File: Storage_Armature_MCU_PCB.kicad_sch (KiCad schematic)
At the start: 71 parts, among them Q1 20N06, U14 USBLC6-2P6, U4 ADP3338AKCZ-3.3RL7, U5 ADP3338AKCZ-3.3RL7

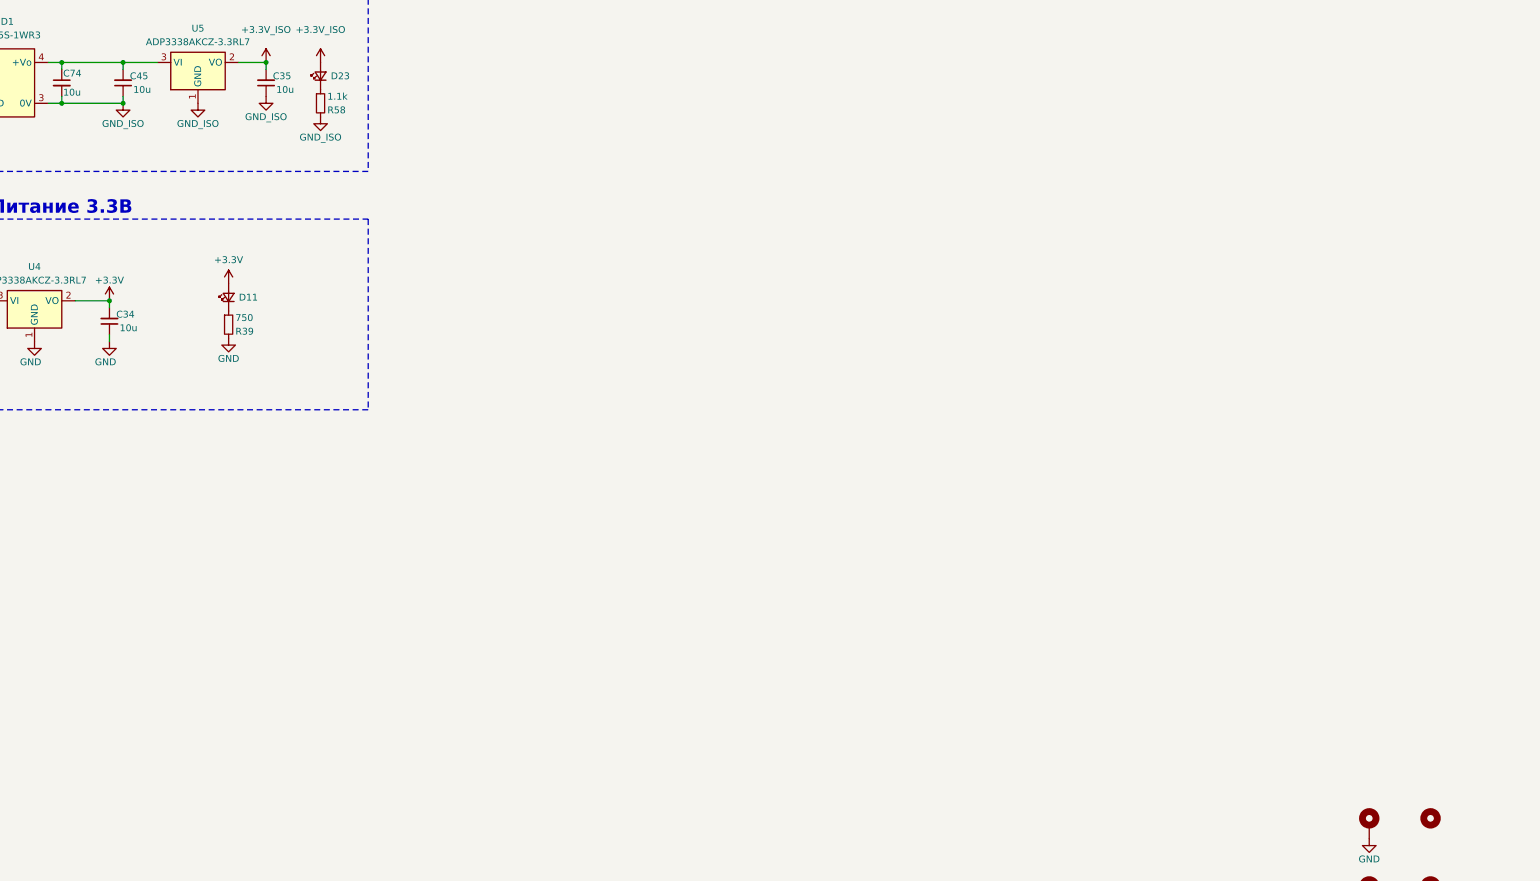
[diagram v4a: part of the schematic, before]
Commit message: VER1.0: объединил земли датчиков и 24В
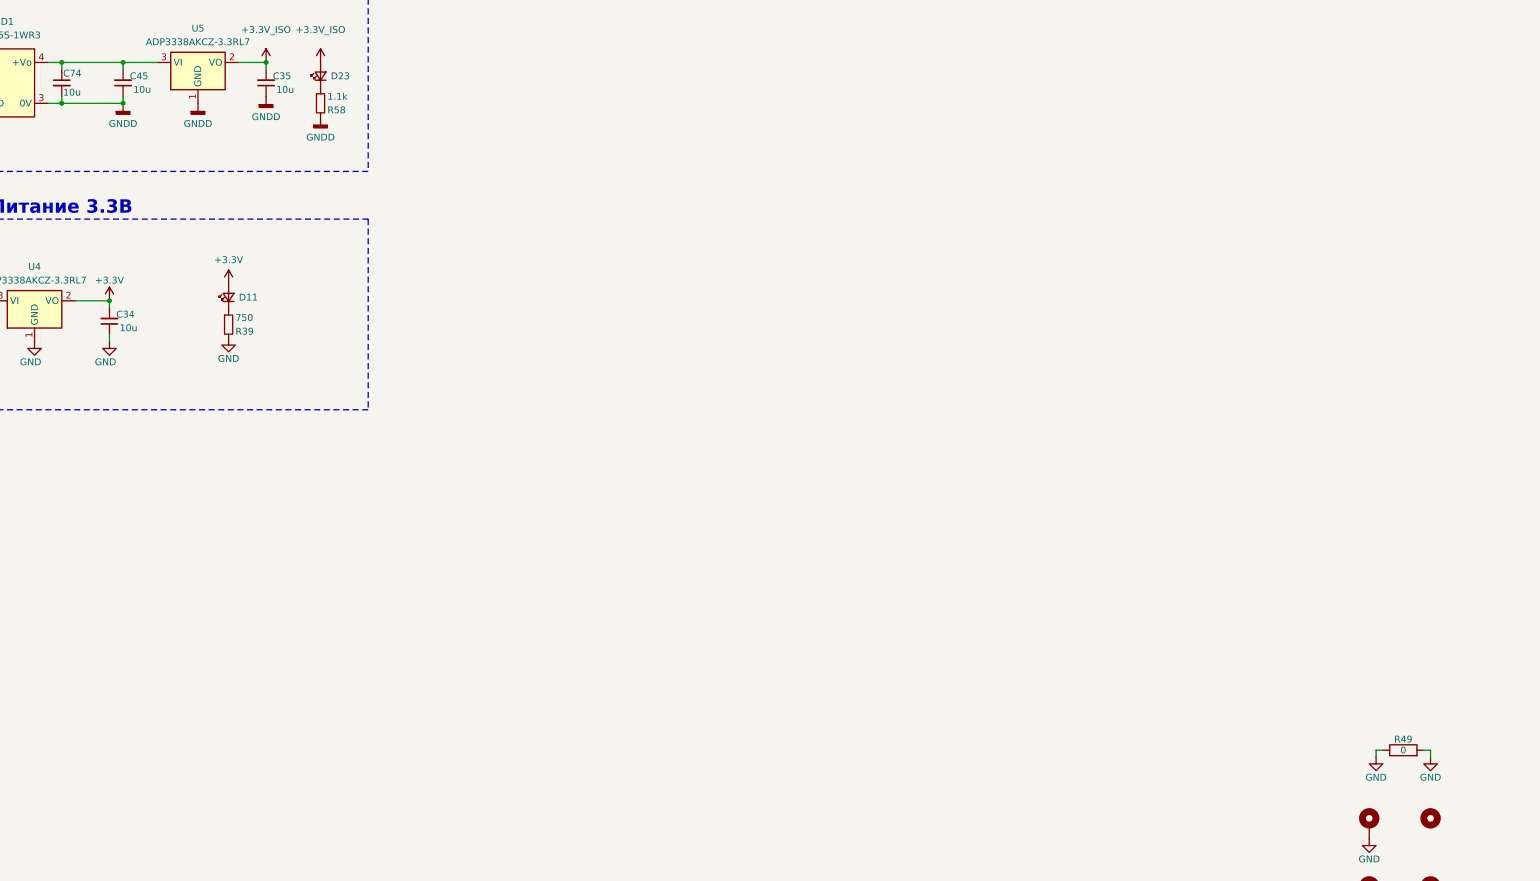
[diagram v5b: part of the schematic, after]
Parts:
- added R49: 0, Resistor_SMD:R_2512_6332Metric_Pad1.40x3.35mm_HandSolder, symbol Device:R
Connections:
- net GND_ISO is gone; now on net GNDD: C35.1, C45.1, C74.2, D1.3 (0V), R58.2, U5.1 (GND)
- net GND: now also R49.1, R49.2

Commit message: VER1.0: добавил светодиоды, тестпоинты и мягкий старт 24В
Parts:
- added Q2: 20N06, Package_TO_SOT_SMD:TO-252-2, symbol Transistor_FET:BSP89
- added R78: 470k, Resistor_SMD:R_0805_2012Metric_Pad1.20x1.40mm_HandSolder, symbol Device:R_Small
- R54: value 8.2k -> 4.7k
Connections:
- net GNDD: now also Q2.2 (D); no longer C70.2, D20.2 (A), Q1.3 (S)
- net Sensor_3/P_measure_MCU: now reaches U1.10 (PC2)
- net Sensor_4/P_measure_MCU: now reaches U1.11 (PC3)
- net Sensor_5/P_measure_MCU: now reaches U1.15 (PA1)
- net Sensor_6/P_measure_MCU: now reaches U1.16 (PA2)
- net Sensor_7/P_measure_MCU: now reaches U1.17 (PA3)
- net Sensor_8/P_measure_MCU: now reaches U1.20 (PA4)
- net Solenoid1_MCU: now reaches U1.50 (PA15)
- net Solenoid2_MCU: now reaches U1.51 (PC10)
- net Solenoid3_MCU: now reaches U1.52 (PC11)
- net Solenoid4_MCU: now reaches U1.53 (PC12)
- net Sensor_1/P_measure_MCU: now reaches U1.8 (PC0)
- net Sensor_2/P_measure_MCU: now reaches U1.9 (PC1)
- net at C70.1, D20.1 (K), Q1.1 (G)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: now also Q2.1 (G), R78.1
- new net: C70.2, D20.2 (A), Q1.3 (S), Q2.3 (S), R78.2
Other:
- added sheet Sensor_6 (Measure.kicad_sch)
- added sheet Sensor_7 (Measure.kicad_sch)
- added sheet Sensor_8 (Measure.kicad_sch)
- sheet Sensor_1 ports: added P_measure_MCU; removed none
- sheet Sensor_2 ports: added P_measure_MCU; removed none
- sheet Sensor_3 ports: added P_measure_MCU; removed none
- sheet Sensor_4 ports: added P_measure_MCU; removed none
- sheet Sensor_5 ports: added P_measure_MCU; removed none
- moved on the sheet: C67, C70, D10, D19, D20, J6, Q1, R54, R55

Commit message: VER1.0: добавил RS485, Board ID, вырезы в плате
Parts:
- added C105: 2.2n, Capacitor_SMD:C_1812_4532Metric_Pad1.57x3.40mm_HandSolder, symbol Device:C
- added C106: 10n, Capacitor_SMD:C_0805_2012Metric_Pad1.18x1.45mm_HandSolder, symbol Device:C_Small
- added C107: 10u, Capacitor_SMD:C_1206_3216Metric_Pad1.33x1.80mm_HandSolder, symbol Device:C_Small
- added C108: 100n, Capacitor_SMD:C_1206_3216Metric_Pad1.33x1.80mm_HandSolder, symbol Device:C_Small
- added C109, C110: 100n, Capacitor_SMD:C_0805_2012Metric_Pad1.18x1.45mm_HandSolder, symbol Device:C_Small
- added D17: (no value), LED_SMD:LED_0805_2012Metric, symbol Device:LED_Small
- added D18: TD301D485H-A, MORNSUN:TD301D485H-AB, symbol MORNSUN:TD301D485H-AB
- added D21: (no value), Package_TO_SOT_SMD:SOT-23, symbol Power_Protection:NUP2105L
- added J38, J39: (no value), Connector_Molex:Molex_Mini-Fit_Jr_5569-04A2_2x02_P4.20mm_Horizontal, symbol Connector_Generic:Conn_02x02_Odd_Even
- added JP1, JP2, JP3, JP4, JP5, JP6, JP7: Jumper_2_Small_Bridged, Connector_PinHeader_2.54mm:PinHeader_1x02_P2.54mm_Vertical, symbol Jumper:Jumper_2_Small_Bridged
- added L4: (no value), Inductor_SMD:L_CommonModeChoke_TDK_ACM2520-2P, symbol Device:L_Coupled_Small
- added R87: 1k, Resistor_SMD:R_0805_2012Metric_Pad1.20x1.40mm_HandSolder, symbol Device:R_Small
- added R88, R89: 59, Resistor_SMD:R_0805_2012Metric_Pad1.20x1.40mm_HandSolder, symbol Device:R_Small
- added R90, R91: 10k, Resistor_SMD:R_0805_2012Metric_Pad1.20x1.40mm_HandSolder, symbol Device:R_Small
- added TP36, TP37, TP38, TP39, TP40, TP41, TP42, TP43: TestPoint, TestPoint:TestPoint_Loop_D1.80mm_Drill1.0mm_Beaded, symbol Connector:TestPoint
- R49: value 0 -> 1M
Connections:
- net +3.3V: now also C107.1, C108.1, D18.1 (VCC), R90.1, R91.1
- net CANH: now also J34.3 (Pin_3), J35.3 (Pin_3); no longer J34.1 (Pin_1), J35.1 (Pin_1)
- net CANL: now also J34.4 (Pin_4), J35.4 (Pin_4); no longer J34.2 (Pin_2), J35.2 (Pin_2)
- net GND: now also C105.1, C105.2, C107.2, C108.2, C109.2, C110.2, D18.2 (GND), JP3.1 (A), JP3.2 (B), JP6.2 (B), JP7.2 (B), R87.2, TP36.1, TP37.1, TP38.1, TP39.1
- net GND_CAN: now also J34.1 (Pin_1), J34.2 (Pin_2), J35.1 (Pin_1), J35.2 (Pin_2); no longer J34.3 (Pin_3), J34.4 (Pin_4), J35.3 (Pin_3), J35.4 (Pin_4)
- net Solenoid1_MCU: now also TP40.1
- net Solenoid2_MCU: now also TP41.1
- net Solenoid3_MCU: now also TP42.1
- net Solenoid4_MCU: now also TP43.1
- net at U1.2 (PC13): now also D17.2 (A); no longer D7.2 (A)
- net at U1.26 (PB0): now also C109.1, JP6.1 (A), R90.2
- net at U1.27 (PB1): now also C110.1, JP7.1 (A), R91.2
- net at U1.3 (PC14): now also D7.2 (A)
- net RS_TXD_MCU: now reaches U1.42 (PA9)
- net RS_TXD_MCU: now also D18.3 (TXD)
- net RS_RXD_MCU: now reaches U1.43 (PA10)
- net RS_RXD_MCU: now also D18.4 (RXD)
- net at D12.6 (CANL), L1.2: now also JP2.2 (B); no longer R40.1
- net at D12.7 (CANH), L1.1: now also JP1.1 (A); no longer R37.2
- new net: JP2.1 (A), R40.1
- new net: D18.9 (A), JP4.1 (A), L4.2
- new net: JP4.2 (B), R88.2
- new net: D17.1 (K), R87.1
- new net: JP1.2 (B), R37.2
- new net: JP5.1 (A), R89.1
- new net: D18.8 (B), JP5.2 (B), L4.1
- new net: C106.1, R88.1, R89.2
- new net A: D21.1 (K), J38.4 (Pin_4), J39.4 (Pin_4), L4.3
- new net B: D21.2 (K), J38.3 (Pin_3), J39.3 (Pin_3), L4.4
- new net GND_RS485: C106.2, D18.10 (RGND), D21.3 (A), J38.1 (Pin_1), J38.2 (Pin_2), J39.1 (Pin_1), J39.2 (Pin_2)
- no-connect marks 11 -> 10
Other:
- note added: "RS-485"
- moved on the sheet: C49, D14, J34, J35, L1, R37, R40

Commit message: VER1.0: добавил сухие контакты и логотип
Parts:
- added C111, C112, C113: 100n, Capacitor_SMD:C_0805_2012Metric_Pad1.18x1.45mm_HandSolder, symbol Device:C_Small
- added J2: ERROR, Connector_Molex:Molex_Mini-Fit_Jr_5569-06A2_2x03_P4.20mm_Horizontal, symbol Connector_Generic:Conn_02x03_Top_Bottom
- added R92, R94, R95: 3.3k, Resistor_SMD:R_1206_3216Metric_Pad1.30x1.75mm_HandSolder, symbol Device:R
- added R93, R96, R97: 10k, Resistor_SMD:R_0805_2012Metric_Pad1.20x1.40mm_HandSolder, symbol Device:R_Small
- added U22: LTV-247, Package_SO:SOP-16_4.4x10.4mm_P1.27mm, symbol Isolator:LTV-247
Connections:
- net +24V: now also J2.1 (Pin_1), J2.2 (Pin_2), J2.3 (Pin_3)
- net +3.3V: now also R93.2, R96.2, R97.2
- net GND: now also C111.2, C112.2, C113.2, U22.11, U22.13, U22.15; no longer C105.1, H2.1, JP3.1 (A), R49.1
- net GNDD: now also U22.2, U22.4, U22.6
- net ERROR_LvL1: now reaches U1.21 (PA5)
- net ERROR_LvL1: now also C111.1, R93.1, U22.12
- net ERROR_LvL2: now reaches U1.22 (PA6)
- net ERROR_LvL2: now also C112.1, R96.1, U22.14
- net ERROR_LvL3: now reaches U1.23 (PA7)
- net ERROR_LvL3: now also C113.1, R97.1, U22.16
- new net: C105.1, H2.1, JP3.1 (A), R49.1
- new net: R95.2, U22.1
- new net: R94.2, U22.3
- new net: R92.2, U22.5
- new net ERROR_LvL1_IN: J2.4 (Pin_4), R92.1
- new net ERROR_LvL2_IN: J2.5 (Pin_5), R94.1
- new net ERROR_LvL3_IN: J2.6 (Pin_6), R95.1
- no-connect marks 10 -> 14
